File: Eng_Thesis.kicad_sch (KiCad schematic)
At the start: 33 parts, among them J1 ST_Llink, J2 Conn_02x07_Counter_Clockwise, J3 Conn_02x07_Counter_Clockwise, J4 Conn_02x07_Counter_Clockwise, J5 Conn_01x02_Socket, SW1 MODBUS_ADDR, SW2 RESET, U1 SN75176AD, U2 STM32F030C8Tx, Y1 8MHz

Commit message: Footprints and elements update
Added another batch of footprints and links to the elements. More coming soon.
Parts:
- C1, C2, C3, C4, C9: footprint Capacitor_SMD:C_0201_0603Metric_Pad0.64x0.40mm_HandSolder -> Capacitor_SMD:C_0603_1608Metric_Pad1.08x0.95mm_HandSolder
- JP1: footprint (none) -> Jumper:SolderJumper-3_P1.3mm_Bridged2Bar12_Pad1.0x1.5mm
- R2, R7: footprint (none) -> Resistor_SMD:R_0603_1608Metric_Pad0.98x0.95mm_HandSolder
- SW1: footprint (none) -> LibLoader:SDA08H1BD
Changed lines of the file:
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@@
       (effects (font (size 1.27 1.27)) (justify left))
     )
-    (property "Footprint" "Capacitor_SMD:C_0201_0603Metric_Pad0.64x0.40mm_HandSolder" (at 77.1652 69.85 0)
+    (property "Footprint" "Capacitor_SMD:C_0603_1608Metric_Pad1.08x0.95mm_HandSolder" (at 77.1652 69.85 0)
       (effects (font (size 1.27 1.27)) hide)
     )
@@
       (effects (font (size 1.27 1.27)))
     )
-    (property "Footprint" "" (at 109.22 161.29 0)
+    (property "Footprint" "Jumper:SolderJumper-3_P1.3mm_Bridged2Bar12_Pad1.0x1.5mm" (at 109.22 161.29 0)
       (effects (font (size 1.27 1.27)) hide)
     )
@@
       (effects (font (size 1.27 1.27)) (justify left))
     )
-    (property "Footprint" "Capacitor_SMD:C_0201_0603Metric_Pad0.64x0.40mm_HandSolder" (at 97.4852 69.85 0)
+    (property "Footprint" "Capacitor_SMD:C_0603_1608Metric_Pad1.08x0.95mm_HandSolder" (at 97.4852 69.85 0)
       (effects (font (size 1.27 1.27)) hide)
     )
@@
       (effects (font (size 1.27 1.27)) (justify left))
     )
-    (property "Footprint" "" (at 101.092 173.99 90)
+    (property "Footprint" "Resistor_SMD:R_0603_1608Metric_Pad0.98x0.95mm_HandSolder" (at 101.092 173.99 90)
       (effects (font (size 1.27 1.27)) hide)
     )
@@
         (path "/97bd1b5a-123d-47f8-a974-72569e0e2197"
           (reference "#PWR030") (unit 1)
-        )
-      )
-    )
-  )
-  (symbol (lib_id "Device:R") (at 101.6 114.3 0) (unit 1)
-    (in_bom yes) (on_board yes) (dnp no) (fields_autoplaced)
-    (property "Reference" "R1" (at 104.14 113.03 0)
-      (effects (font (size 1.27 1.27)) (justify left))
-    )
-    (property "Value" "4.7k" (at 104.14 115.57 0)
-      (effects (font (size 1.27 1.27)) (justify left))
-    )
-    (property "Footprint" "Resistor_SMD:R_0603_1608Metric_Pad0.98x0.95mm_HandSolder" (at 99.822 114.3 90)
-      (effects (font (size 1.27 1.27)) hide)
-    )
-    (property "Datasheet" "https://www.tme.eu/pl/details/crgcq0603j4k7/rezystory-smd/te-connectivity/2-2176340-3/" (at 101.6 114.3 0)
-      (effects (font (size 1.27 1.27)) hide)
-    )
-    (pin "1")
-    (pin "2")
-    (instances
-      (project "Eng_Thesis"
-        (path "/97bd1b5a-123d-47f8-a974-72569e0e2197"
-          (reference "R1") (unit 1)
         )
       )
@@
       (effects (font (size 1.27 1.27)) (justify left))
     )
-    (property "Footprint" "Capacitor_SMD:C_0201_0603Metric_Pad0.64x0.40mm_HandSolder" (at 87.3252 69.85 0)
+    (property "Footprint" "Capacitor_SMD:C_0603_1608Metric_Pad1.08x0.95mm_HandSolder" (at 87.3252 69.85 0)
       (effects (font (size 1.27 1.27)) hide)
     )
@@
       (effects (font (size 1.27 1.27)))
     )
-    (property "Footprint" "" (at 199.39 105.41 0)
+    (property "Footprint" "LibLoader:SDA08H1BD" (at 199.39 105.41 0)
       (effects (font (size 1.27 1.27)) hide)
     )
@@
       (effects (font (size 1.27 1.27)) (justify left))
     )
-    (property "Footprint" "Capacitor_SMD:C_0201_0603Metric_Pad0.64x0.40mm_HandSolder" (at 107.6452 69.85 0)
+    (property "Footprint" "Capacitor_SMD:C_0603_1608Metric_Pad1.08x0.95mm_HandSolder" (at 107.6452 69.85 0)
       (effects (font (size 1.27 1.27)) hide)
     )
@@
     )
   )
+  (symbol (lib_id "Device:R") (at 101.6 114.3 0) (unit 1)
+    (in_bom yes) (on_board yes) (dnp no) (fields_autoplaced)
+    (property "Reference" "R1" (at 104.14 113.03 0)
+      (effects (font (size 1.27 1.27)) (justify left))
+    )
+    (property "Value" "4.7k" (at 104.14 115.57 0)
+      (effects (font (size 1.27 1.27)) (justify left))
+    )
+    (property "Footprint" "Resistor_SMD:R_0603_1608Metric_Pad0.98x0.95mm_HandSolder" (at 99.822 114.3 90)
+      (effects (font (size 1.27 1.27)) hide)
+    )
+    (property "Datasheet" "" (at 101.6 114.3 0)
+      (effects (font (size 1.27 1.27)) hide)
+    )
+    (pin "1")
+    (pin "2")
+    (instances
+      (project "Eng_Thesis"
+        (path "/97bd1b5a-123d-47f8-a974-72569e0e2197"
+          (reference "R1") (unit 1)
+        )
+      )
+    )
+  )
   (symbol (lib_id "power:+3V3") (at 214.63 24.13 0) (unit 1)
     (in_bom yes) (on_board yes) (dnp no) (fields_autoplaced)
@@
       (effects (font (size 1.27 1.27)))
     )
-    (property "Footprint" "Capacitor_SMD:C_0201_0603Metric_Pad0.64x0.40mm_HandSolder" (at 210.82 47.2948 0)
+    (property "Footprint" "Capacitor_SMD:C_0603_1608Metric_Pad1.08x0.95mm_HandSolder" (at 210.82 47.2948 0)
       (effects (font (size 1.27 1.27)) hide)
     )
@@
       (effects (font (size 1.27 1.27)) (justify left))
     )
-    (property "Footprint" "" (at 155.702 58.42 90)
-      (effects (font (size 1.27 1.27)) hide)
-    )
+    (property "Footprint" "Resistor_SMD:R_0603_1608Metric_Pad0.98x0.95mm_HandSolder" (at 155.702 58.42 90)
+      (effects (font (size 1.27 1.27)) hide)
+    )

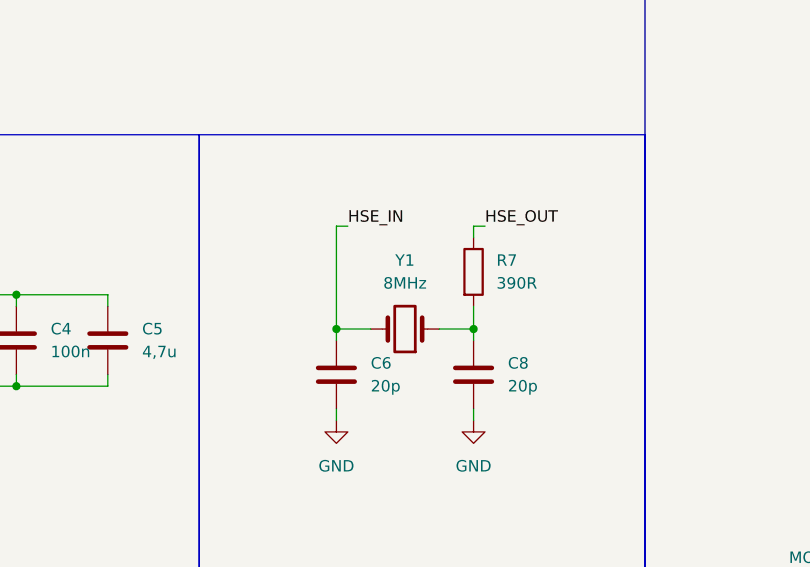
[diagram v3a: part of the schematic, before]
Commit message: 1st complete version of schematic with footprints
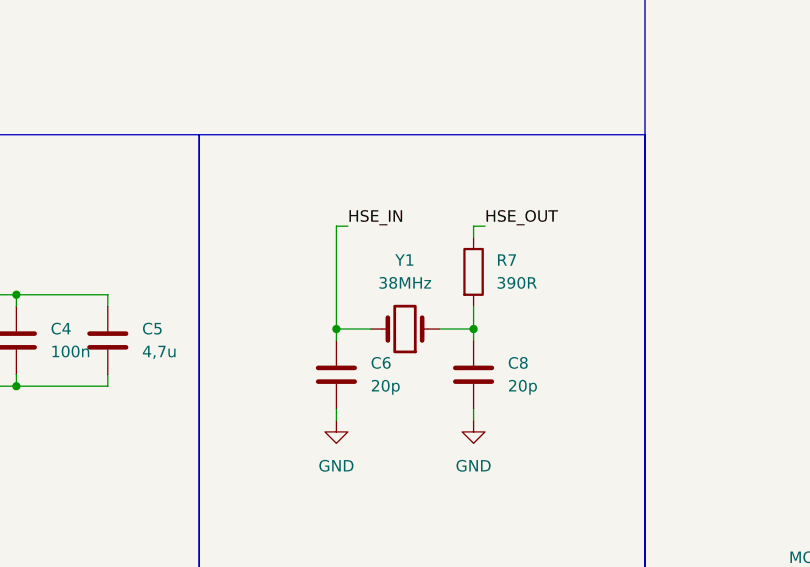
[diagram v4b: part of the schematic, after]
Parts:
- J5: footprint (none) -> LibLoader:TB508P2PBL
- SW2: footprint (none) -> Button_Switch_SMD:SW_Push_1P1T_NO_6x6mm_H9.5mm
- Y1: value 8MHz -> 38MHz; footprint (none) -> Crystal:Crystal_SMD_HC49-SD_HandSoldering
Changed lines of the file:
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@@
       (effects (font (size 1.27 1.27)))
     )
-    (property "Value" "8MHz" (at 149.86 59.69 0)
-      (effects (font (size 1.27 1.27)))
-    )
-    (property "Footprint" "" (at 149.86 64.77 0)
-      (effects (font (size 1.27 1.27)) hide)
-    )
-    (property "Datasheet" "~" (at 149.86 64.77 0)
+    (property "Value" "38MHz" (at 149.86 59.69 0)
+      (effects (font (size 1.27 1.27)))
+    )
+    (property "Footprint" "Crystal:Crystal_SMD_HC49-SD_HandSoldering" (at 149.86 64.77 0)
+      (effects (font (size 1.27 1.27)) hide)
+    )
+    (property "Datasheet" "https://www.tme.eu/pl/details/38m-49smd-sr/rezonatory-kwarcowe-smd/sr-passives/" (at 149.86 64.77 0)
       (effects (font (size 1.27 1.27)) hide)
     )
@@
       (effects (font (size 1.27 1.27)))
     )
-    (property "Footprint" "" (at 207.01 31.75 0)
+    (property "Footprint" "Button_Switch_SMD:SW_Push_1P1T_NO_6x6mm_H9.5mm" (at 207.01 31.75 0)
       (effects (font (size 1.27 1.27)) hide)
     )
@@
       (effects (font (size 1.27 1.27)) (justify left))
     )
-    (property "Footprint" "" (at 139.7 179.07 0)
-      (effects (font (size 1.27 1.27)) hide)
-    )
-    (property "Datasheet" "~" (at 139.7 179.07 0)
-      (effects (font (size 1.27 1.27)) hide)
-    )
+    (property "Footprint" "LibLoader:TB508P2PBL" (at 139.7 179.07 0)
+      (effects (font (size 1.27 1.27)) hide)
+    )
+    (property "Datasheet" "https://www.tme.eu/pl/details/tb-5.08-p-2p_bl/listwy-zaciskowe-do-druku/ninigi/?brutto=1&currency=PLN&gad_source=1&gclid=CjwKCAjwmrqzBhAoEiwAXVpgojoKrkXLDTwjQoFKpdxCaEU1GNU52KAbsTR_a_L-CxTX3f7-0nV2TxoCxK0QAvD_BwE" (at 139.7 179.07 0)
+      (effects (font (size 1.27 1.27)) hide)
+    )

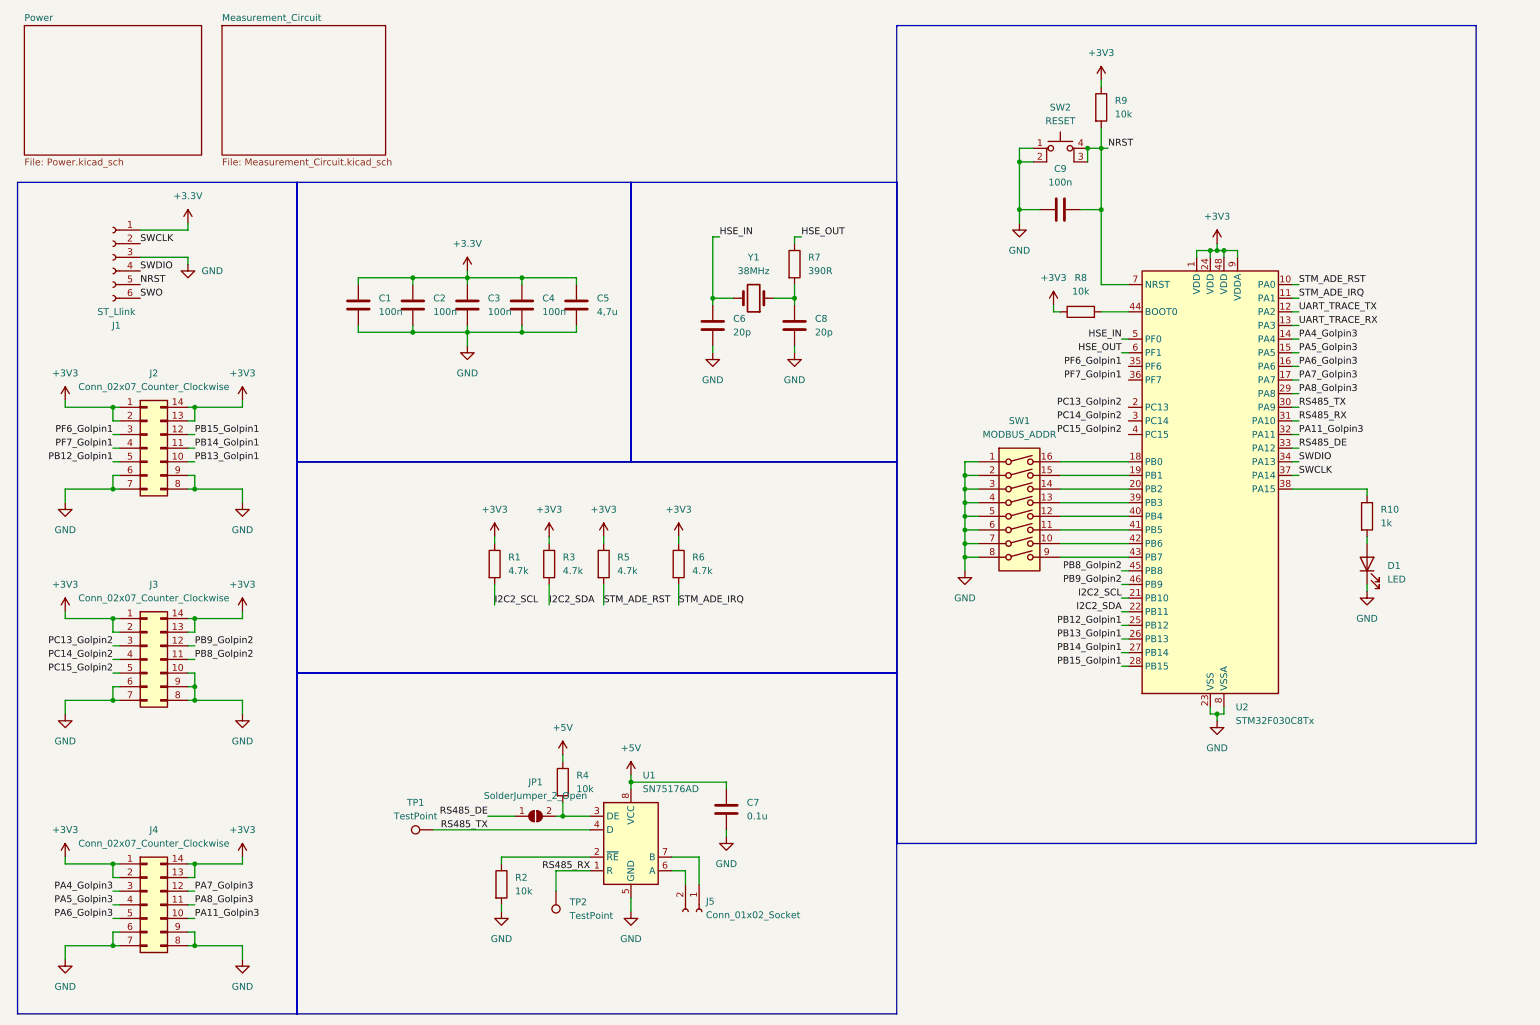
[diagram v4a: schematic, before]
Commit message: Fixes on schematics and footprint update
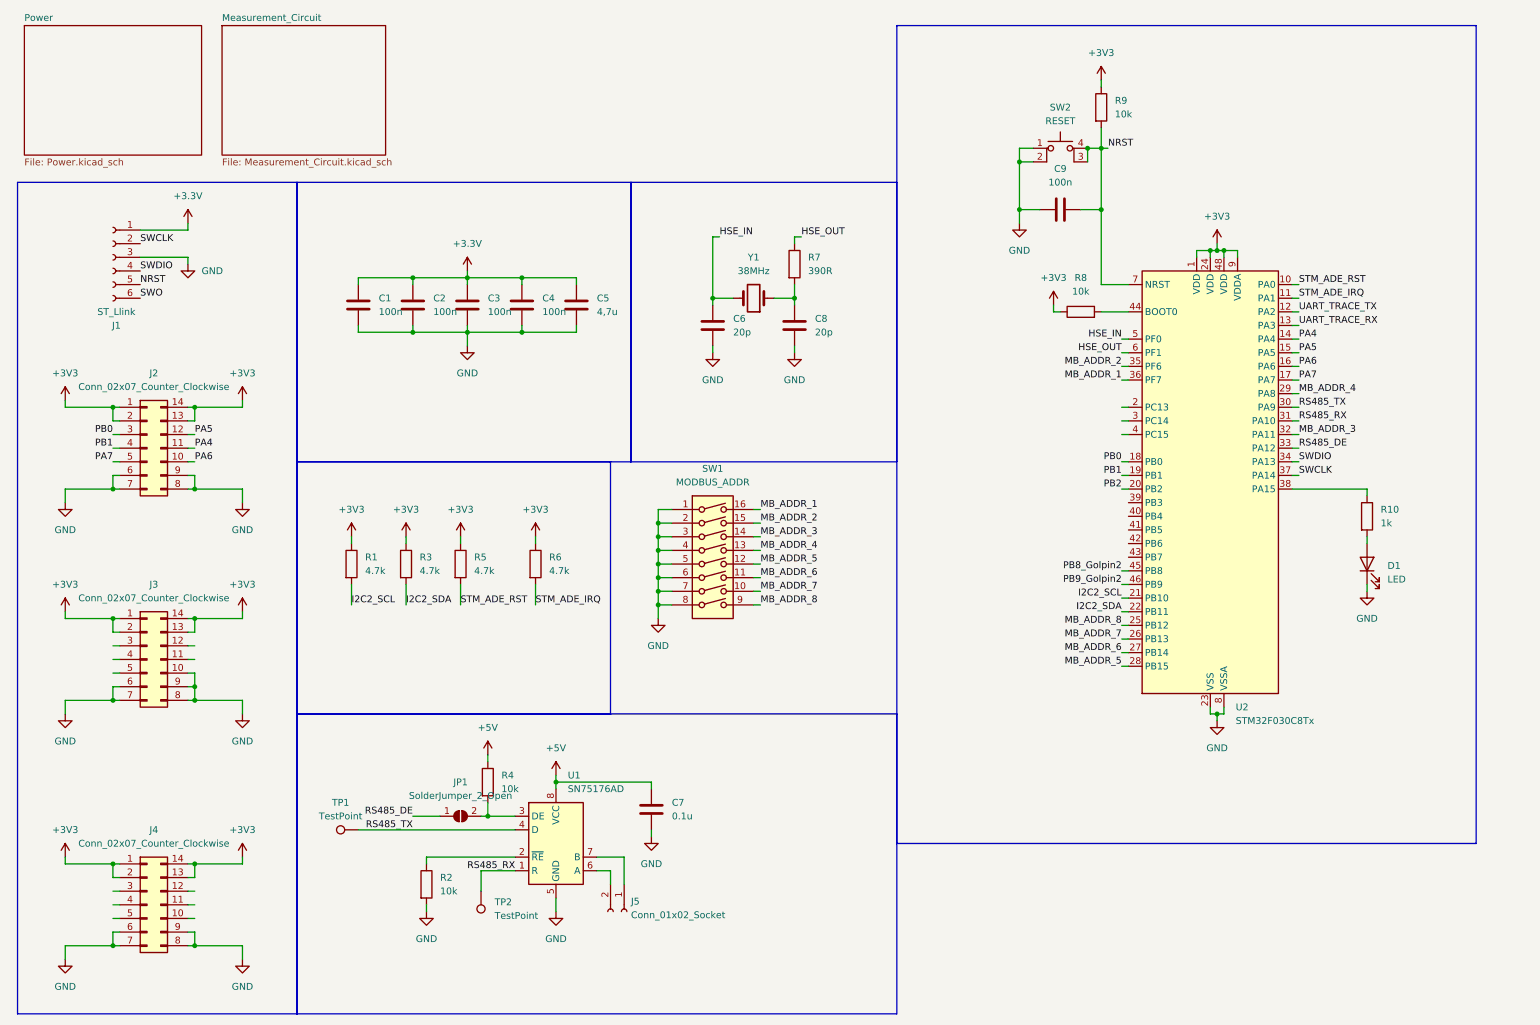
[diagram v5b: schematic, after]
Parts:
- C1, C2, C3, C4, C5, C6, C7, C8, C9: footprint Capacitor_SMD:C_0603_1608Metric_Pad1.08x0.95mm_HandSolder -> Capacitor_SMD:C_0805_2012Metric_Pad1.18x1.45mm_HandSolder
- JP1: footprint Jumper:SolderJumper-3_P1.3mm_Bridged2Bar12_Pad1.0x1.5mm -> Jumper:SolderJumper-2_P1.3mm_Open_TrianglePad1.0x1.5mm
- R1, R10, R2, R3, R4, R5, R6, R7, R8, R9: footprint Resistor_SMD:R_0603_1608Metric_Pad0.98x0.95mm_HandSolder -> Resistor_SMD:R_0805_2012Metric_Pad1.20x1.40mm_HandSolder
- SW2: footprint Button_Switch_SMD:SW_Push_1P1T_NO_6x6mm_H9.5mm -> LibLoader:TL3305BF160QG
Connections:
- net PB8_Golpin2: no longer J3.11 (Pin_11)
- net PB9_Golpin2: no longer J3.12 (Pin_12)
- net MB_ADDR_1: now reaches SW1.16
- net MB_ADDR_1: now also U2.36 (PF7); no longer U2.18 (PB0)
- net MB_ADDR_2: now reaches SW1.15
- net MB_ADDR_2: now also U2.35 (PF6); no longer U2.19 (PB1)
- net MB_ADDR_3: now reaches SW1.14
- net MB_ADDR_3: now also U2.32 (PA11); no longer U2.20 (PB2)
- net at U2.39 (PB3): no longer SW1.13
- net at U2.40 (PB4): no longer SW1.12
- net at U2.41 (PB5): no longer SW1.11
- net at U2.42 (PB6): no longer SW1.10
- net at U2.43 (PB7): no longer SW1.9
- net PA11_Golpin3: no longer names the net of J4.10 (Pin_10)
- net PA11_Golpin3: no longer U2.32 (PA11)
- net PA4_Golpin3: no longer names the net of J4.3 (Pin_3)
- net PA4_Golpin3: no longer U2.14 (PA4)
- net PA5_Golpin3: no longer names the net of J4.4 (Pin_4)
- net PA5_Golpin3: no longer U2.15 (PA5)
- net PA6_Golpin3: no longer names the net of J4.5 (Pin_5)
- net PA6_Golpin3: no longer U2.16 (PA6)
- net PA7_Golpin3: no longer names the net of J4.12 (Pin_12)
- net PA7_Golpin3: no longer U2.17 (PA7)
- net PA8_Golpin3: no longer names the net of J4.11 (Pin_11)
- net PA8_Golpin3: no longer U2.29 (PA8)
- net PB12_Golpin1 renamed MB_ADDR_8
- net MB_ADDR_8: now also SW1.9; no longer J2.5 (Pin_5)
- net PB13_Golpin1 renamed MB_ADDR_7
- net MB_ADDR_7: now also SW1.10; no longer J2.10 (Pin_10)
- net PB14_Golpin1 renamed MB_ADDR_6
- net MB_ADDR_6: now also SW1.11; no longer J2.11 (Pin_11)
- net PB15_Golpin1 renamed MB_ADDR_5
- net MB_ADDR_5: now also SW1.12; no longer J2.12 (Pin_12)
- net PC13_Golpin2: no longer names the net of J3.3 (Pin_3)
- net PC14_Golpin2: no longer names the net of J3.4 (Pin_4)
- net PC15_Golpin2: no longer names the net of J3.5 (Pin_5)
- net PF6_Golpin1 renamed PB0
- net PB0: now also U2.18 (PB0)
- net PF7_Golpin1 renamed PB1
- net PB1: now also U2.19 (PB1)
- new net MB_ADDR_4: SW1.13, U2.29 (PA8)
- new net PA4: J2.11 (Pin_11), U2.14 (PA4)
- new net PA5: J2.12 (Pin_12), U2.15 (PA5)
- new net PA6: J2.10 (Pin_10), U2.16 (PA6)
- new net PA7: J2.5 (Pin_5), U2.17 (PA7)
- new net PB2: U2.20 (PB2)
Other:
- moved on the sheet: C7, J5, JP1, R1, R2, R3, R4, R5, R6, SW1, TP1, TP2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

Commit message: v.0.1
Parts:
- removed C6, C8: 20p, Capacitor_SMD:C_0805_2012Metric_Pad1.18x1.45mm_HandSolder, symbol Device:C
- removed J2, J3, J4: Conn_02x07_Counter_Clockwise, Connector_PinHeader_2.54mm:PinHeader_2x07_P2.54mm_Vertical, symbol Connector_Generic:Conn_02x07_Counter_Clockwise
- removed R7: 390R, Resistor_SMD:R_0805_2012Metric_Pad1.20x1.40mm_HandSolder, symbol Device:R
- removed TP1, TP2: TestPoint, TestPoint:TestPoint_Pad_1.5x1.5mm, symbol Connector:TestPoint
- removed Y1: 38MHz, Crystal:Crystal_SMD_HC49-SD_HandSoldering, symbol Device:Crystal
- added J2: Conn_01x03_Socket, Connector_PinSocket_2.54mm:PinSocket_1x03_P2.54mm_Vertical, symbol Connector:Conn_01x03_Socket
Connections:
- net +3V3 is gone; now on net +3.3V: R1.1, R3.1, R5.1, R6.1, R8.1, R9.1, U2.1 (VDD), U2.24 (VDD), U2.48 (VDD), U2.9 (VDDA)
- net GND: now also J2.3 (Pin_3)
- net UART_TRACE_RX: now also J2.2 (Pin_2)
- net UART_TRACE_TX: now also J2.1 (Pin_1)
- net HSE_IN: no longer names the net of U2.5 (PF0)
- net HSE_OUT: no longer names the net of U2.6 (PF1)
- net I2C2_SCL renamed I2C_SCL
- net I2C2_SDA renamed I2C_SDA
- net PA4: no longer names the net of U2.14 (PA4)
- net PA5: no longer names the net of U2.15 (PA5)
- net PA6: no longer names the net of U2.16 (PA6)
- net PA7: no longer names the net of U2.17 (PA7)
- net PB0: no longer names the net of U2.18 (PB0)
- net PB1: no longer names the net of U2.19 (PB1)
- net PB2: no longer names the net of U2.20 (PB2)
- net PB8_Golpin2: no longer names the net of U2.45 (PB8)
- net PB9_Golpin2: no longer names the net of U2.46 (PB9)
- no-connect marks 0 -> 20
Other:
- sheet Measurement_Circuit ports: added I2C_SCL, I2C_SDA, STM_ADE_IRQ, STM_ADE_RST; removed none
